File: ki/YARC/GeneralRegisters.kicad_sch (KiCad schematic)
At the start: 12 parts, among them U71 74LS670, U72 74LS670, U73 74LS157, U74 74LS670, U75 74LS670, U76 74LS157, U77 74LS670, U78 74LS670, U79 74LS157, U80 74LS670, U81 74LS670, U82 74LS157

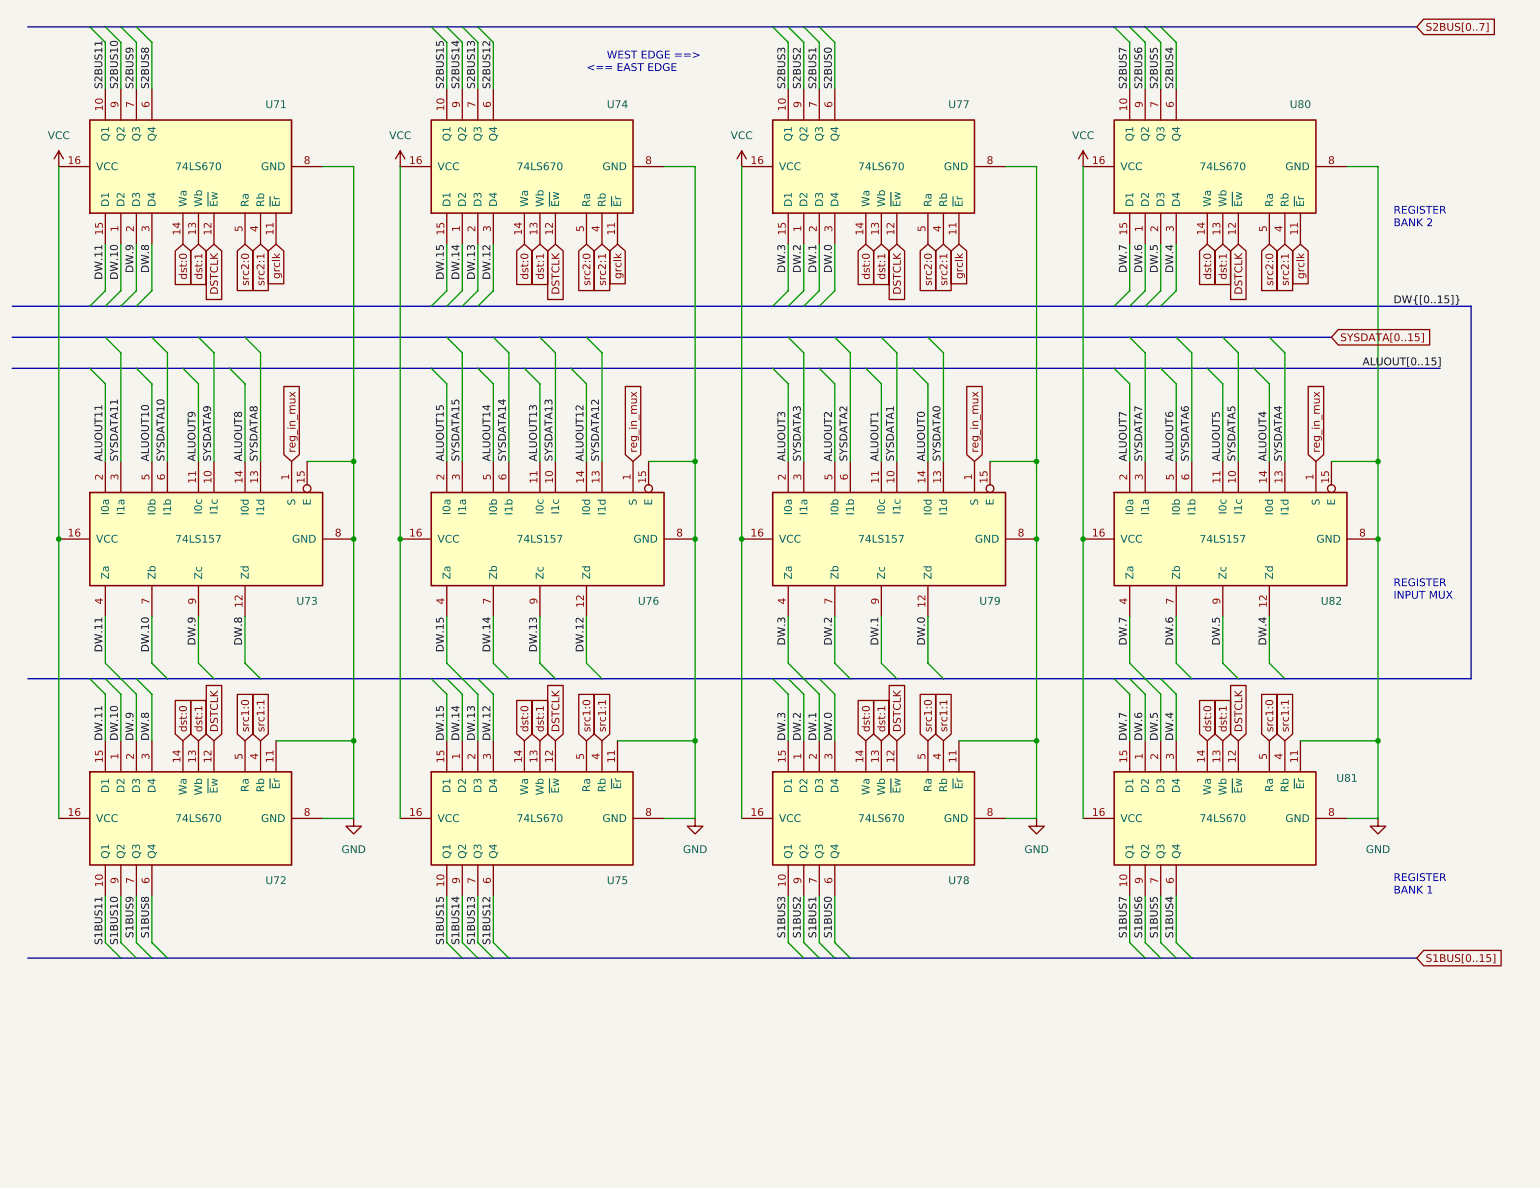
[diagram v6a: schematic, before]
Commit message: Ongoing fixes for ERC errors
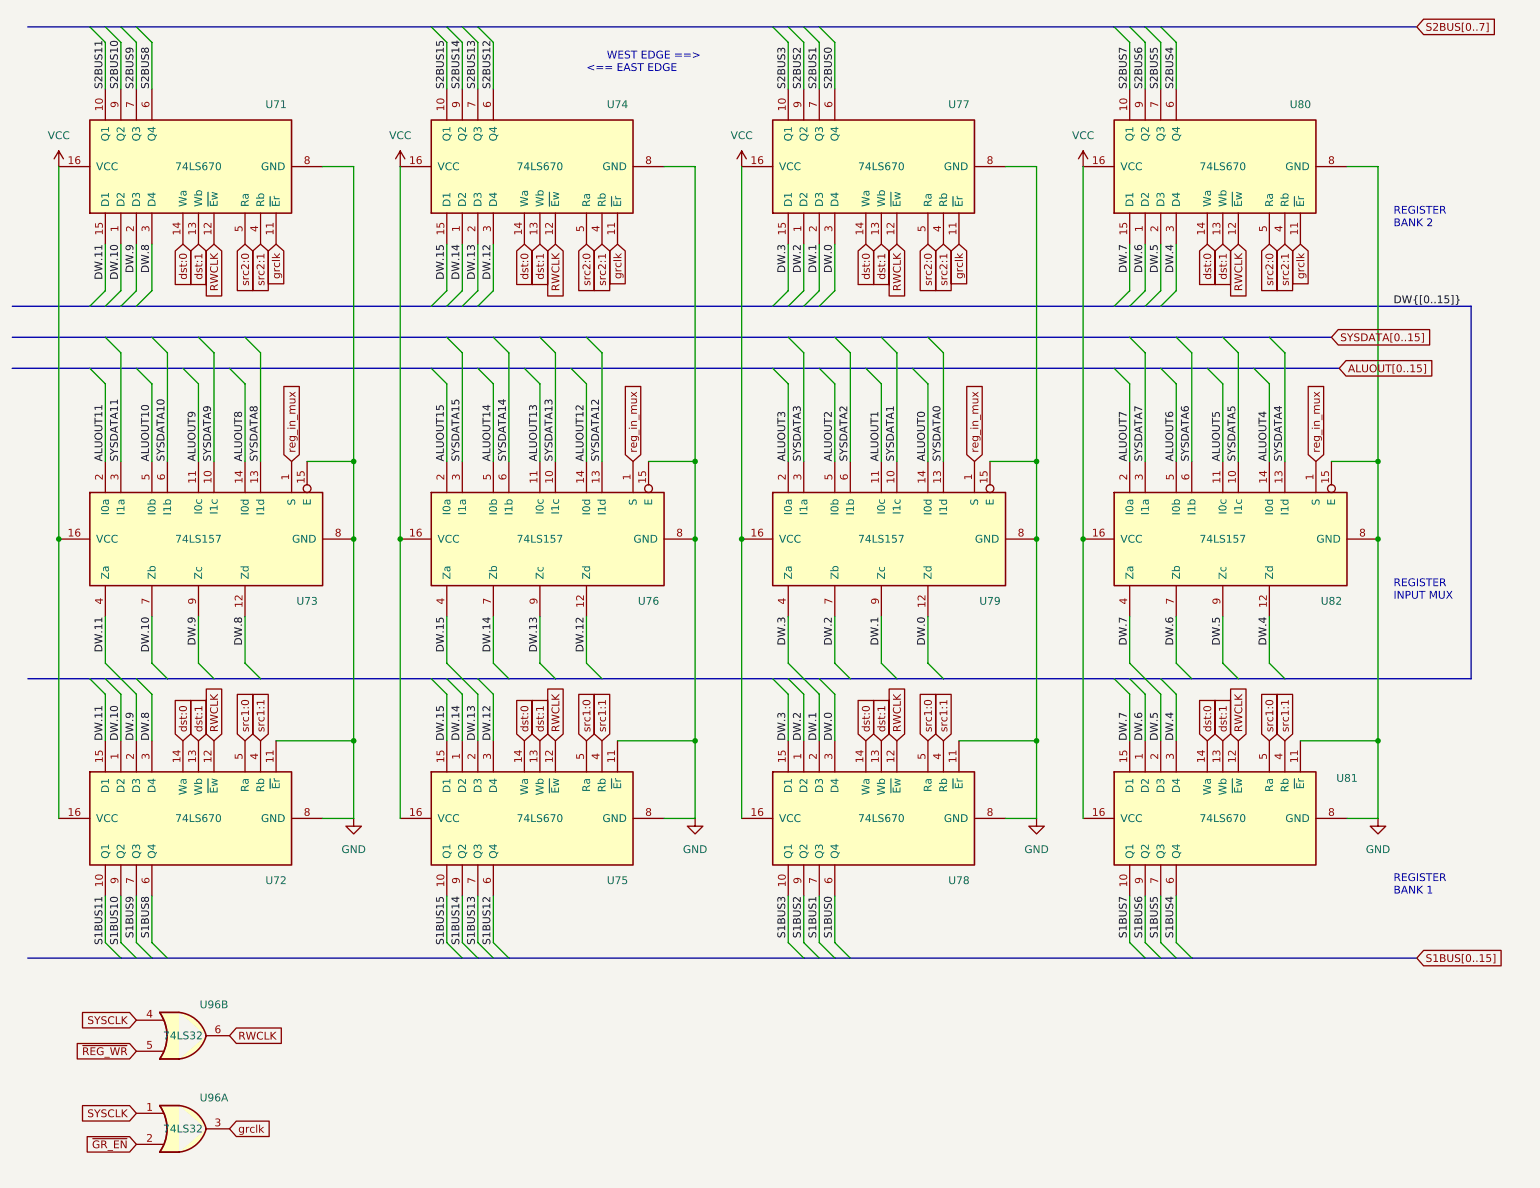
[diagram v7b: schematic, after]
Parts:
- added U96: 74LS32, symbol 74xx:74LS32
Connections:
- net grclk: now also U96.3
- net DSTCLK renamed RWCLK
- net RWCLK: now also U96.6
- new net SYSCLK: U96.1, U96.4
- new net ~{GR_EN}: U96.2
- new net ~{REG_WR}: U96.5
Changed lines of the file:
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@@
     (stroke (width 0) (type default))
   )
-  (bus (pts (xy 218.44 71.12) (xy 248.92 71.12))
+  (bus (pts (xy 218.44 71.12) (xy 232.41 71.12))
     (stroke (width 0) (type default))
   )
@@
     (effects (font (size 1.27 1.27)) (justify right bottom))
   )
-  (label "ALUOUT[0..15]" (at 236.22 71.12 0) (fields_autoplaced)
-    (effects (font (size 1.27 1.27)) (justify left bottom))
-  )
   (label "ALUOUT5" (at 213.36 86.36 90) (fields_autoplaced)
     (effects (font (size 1.27 1.27)) (justify left bottom))
@@
     )
   )
-  (global_label "DSTCLK" (shape input) (at 104.14 132.08 90) (fields_autoplaced)
-    (effects (font (size 1.27 1.27)) (justify left))
-    (property "Intersheetrefs" "${INTERSHEET_REFS}" (at 104.0606 122.6517 90)
+  (global_label "SYSCLK" (shape input) (at 35.56 177.8 180) (fields_autoplaced)
+    (effects (font (size 1.27 1.27)) (justify right))
+    (property "Intersheetrefs" "${INTERSHEET_REFS}" (at 26.0712 177.7206 0)
+      (effects (font (size 1.27 1.27)) (justify right) hide)
+    )
+  )
+  (global_label "RWCLK" (shape input) (at 104.14 132.08 90) (fields_autoplaced)
+    (effects (font (size 1.27 1.27)) (justify left))
+    (property "Intersheetrefs" "${INTERSHEET_REFS}" (at 104.14 122.8053 90)
       (effects (font (size 1.27 1.27)) (justify left) hide)
     )
@@
     )
   )
-  (global_label "DSTCLK" (shape input) (at 160.02 50.8 270) (fields_autoplaced)
-    (effects (font (size 1.27 1.27)) (justify right))
-    (property "Intersheetrefs" "${INTERSHEET_REFS}" (at 159.9406 60.2283 90)
+  (global_label "RWCLK" (shape input) (at 160.02 50.8 270) (fields_autoplaced)
+    (effects (font (size 1.27 1.27)) (justify right))
+    (property "Intersheetrefs" "${INTERSHEET_REFS}" (at 160.02 60.0747 90)
       (effects (font (size 1.27 1.27)) (justify right) hide)
     )
@@
     )
   )
-  (global_label "DSTCLK" (shape input) (at 48.26 132.08 90) (fields_autoplaced)
-    (effects (font (size 1.27 1.27)) (justify left))
-    (property "Intersheetrefs" "${INTERSHEET_REFS}" (at 48.1806 122.6517 90)
-      (effects (font (size 1.27 1.27)) (justify left) hide)
-    )
-  )
-  (global_label "DSTCLK" (shape input) (at 104.14 50.8 270) (fields_autoplaced)
-    (effects (font (size 1.27 1.27)) (justify right))
-    (property "Intersheetrefs" "${INTERSHEET_REFS}" (at 104.0606 60.2283 90)
+  (global_label "RWCLK" (shape input) (at 48.26 132.08 90) (fields_autoplaced)
+    (effects (font (size 1.27 1.27)) (justify left))
+    (property "Intersheetrefs" "${INTERSHEET_REFS}" (at 48.26 122.8053 90)
+      (effects (font (size 1.27 1.27)) (justify left) hide)
+    )
+  )
+  (global_label "RWCLK" (shape input) (at 104.14 50.8 270) (fields_autoplaced)
+    (effects (font (size 1.27 1.27)) (justify right))
+    (property "Intersheetrefs" "${INTERSHEET_REFS}" (at 104.14 60.0747 90)
       (effects (font (size 1.27 1.27)) (justify right) hide)
     )
@@
     )
   )
+  (global_label "RWCLK" (shape input) (at 50.8 180.34 0) (fields_autoplaced)
+    (effects (font (size 1.27 1.27)) (justify left))
+    (property "Intersheetrefs" "${INTERSHEET_REFS}" (at 60.0747 180.34 0)
+      (effects (font (size 1.27 1.27)) (justify left) hide)
+    )
+  )
   (global_label "src2:1" (shape input) (at 55.88 50.8 270) (fields_autoplaced)
     (effects (font (size 1.27 1.27)) (justify right))
@@
     )
   )
+  (global_label "ALUOUT[0..15]" (shape input) (at 232.41 71.12 0) (fields_autoplaced)
+    (effects (font (size 1.27 1.27)) (justify left))
+    (property "Intersheetrefs" "${INTERSHEET_REFS}" (at 249.0025 71.12 0)
+      (effects (font (size 1.27 1.27)) (justify left) hide)
+    )
+  )
   (global_label "src1:0" (shape input) (at 165.1 132.08 90) (fields_autoplaced)
     (effects (font (size 1.27 1.27)) (justify left))
@@
     )
   )
-  (global_label "DSTCLK" (shape input) (at 160.02 132.08 90) (fields_autoplaced)
-    (effects (font (size 1.27 1.27)) (justify left))
-    (property "Intersheetrefs" "${INTERSHEET_REFS}" (at 159.9406 122.6517 90)
+  (global_label "RWCLK" (shape input) (at 160.02 132.08 90) (fields_autoplaced)
+    (effects (font (size 1.27 1.27)) (justify left))
+    (property "Intersheetrefs" "${INTERSHEET_REFS}" (at 160.02 122.8053 90)
       (effects (font (size 1.27 1.27)) (justify left) hide)
     )
@@
     )
   )
-  (global_label "DSTCLK" (shape input) (at 215.9 50.8 270) (fields_autoplaced)
-    (effects (font (size 1.27 1.27)) (justify right))
-    (property "Intersheetrefs" "${INTERSHEET_REFS}" (at 215.8206 60.2283 90)
+  (global_label "RWCLK" (shape input) (at 215.9 50.8 270) (fields_autoplaced)
+    (effects (font (size 1.27 1.27)) (justify right))
+    (property "Intersheetrefs" "${INTERSHEET_REFS}" (at 215.9 60.0747 90)
+      (effects (font (size 1.27 1.27)) (justify right) hide)
+    )
+  )
+  (global_label "SYSCLK" (shape input) (at 35.56 193.04 180) (fields_autoplaced)
+    (effects (font (size 1.27 1.27)) (justify right))
+    (property "Intersheetrefs" "${INTERSHEET_REFS}" (at 26.0712 192.9606 0)
       (effects (font (size 1.27 1.27)) (justify right) hide)
     )
@@
     )
   )
+  (global_label "grclk" (shape input) (at 50.8 195.58 0) (fields_autoplaced)
+    (effects (font (size 1.27 1.27)) (justify left))
+    (property "Intersheetrefs" "${INTERSHEET_REFS}" (at 57.9302 195.5006 0)
+      (effects (font (size 1.27 1.27)) (justify left) hide)
+    )
+  )
   (global_label "dst:1" (shape input) (at 101.6 50.8 270) (fields_autoplaced)
     (effects (font (size 1.27 1.27)) (justify right))
@@
     )
   )
-  (global_label "DSTCLK" (shape input) (at 48.26 50.8 270) (fields_autoplaced)
-    (effects (font (size 1.27 1.27)) (justify right))
-    (property "Intersheetrefs" "${INTERSHEET_REFS}" (at 48.1806 60.2283 90)
+  (global_label "RWCLK" (shape input) (at 48.26 50.8 270) (fields_autoplaced)
+    (effects (font (size 1.27 1.27)) (justify right))
+    (property "Intersheetrefs" "${INTERSHEET_REFS}" (at 48.26 60.0747 90)
+      (effects (font (size 1.27 1.27)) (justify right) hide)
+    )
+  )
+  (global_label "~{REG_WR}" (shape input) (at 35.56 182.88 180) (fields_autoplaced)
+    (effects (font (size 1.27 1.27)) (justify right))
+    (property "Intersheetrefs" "${INTERSHEET_REFS}" (at 25.1968 182.88 0)
       (effects (font (size 1.27 1.27)) (justify right) hide)
     )
@@
     )
   )
-  (global_label "DSTCLK" (shape input) (at 215.9 132.08 90) (fields_autoplaced)
-    (effects (font (size 1.27 1.27)) (justify left))
-    (property "Intersheetrefs" "${INTERSHEET_REFS}" (at 215.8206 122.6517 90)
-      (effects (font (size 1.27 1.27)) (justify left) hide)
+  (global_label "RWCLK" (shape input) (at 215.9 132.08 90) (fields_autoplaced)
+    (effects (font (size 1.27 1.27)) (justify left))
+    (property "Intersheetrefs" "${INTERSHEET_REFS}" (at 215.9 122.8053 90)
+      (effects (font (size 1.27 1.27)) (justify left) hide)
+    )
+  )
+  (global_label "~{GR_EN}" (shape input) (at 35.56 198.12 180) (fields_autoplaced)
+    (effects (font (size 1.27 1.27)) (justify right))
+    (property "Intersheetrefs" "${INTERSHEET_REFS}" (at 27.1598 198.0406 0)
+      (effects (font (size 1.27 1.27)) (justify right) hide)
     )
   )
@@
     )
   )
+  (symbol (lib_id "74xx:74LS32") (at 43.18 180.34 0) (unit 2)
+    (in_bom yes) (on_board yes) (dnp no)
+    (property "Reference" "U96" (at 48.26 175.26 0)
+      (effects (font (size 1.27 1.27)))
+    )
+    (property "Value" "74LS32" (at 43.18 180.34 0)
+      (effects (font (size 1.27 1.27)))
+    )
+    (property "Footprint" "" (at 43.18 180.34 0)
+      (effects (font (size 1.27 1.27)) hide)
+    )
+    (property "Datasheet" "http://www.ti.com/lit/gpn/sn74LS32" (at 43.18 180.34 0)
+      (effects (font (size 1.27 1.27)) hide)
+    )
+    (pin "1")
+    (pin "2")
+    (pin "3")
+    (pin "4")
+    (pin "5")
+    (pin "6")
+    (pin "10")
+    (pin "8")
+    (pin "9")
+    (pin "11")
+    (pin "12")
+    (pin "13")
+    (pin "14")
+    (pin "7")
+    (instances
+      (project "YARC"
+        (path "/22e0f8e1-b0d7-4d47-bb7c-8ef04cd95fca/abd64d43-20ca-4b37-94fd-5fc041c76dd4"
+          (reference "U96") (unit 2)
+        )
+        (path "/22e0f8e1-b0d7-4d47-bb7c-8ef04cd95fca/08911a09-4c52-4bc8-9a9a-ff564ff87689"
+          (reference "U147") (unit 2)
+        )
+      )
+    )
+  )
   (symbol (lib_id "power:VCC") (at 134.62 38.1 0) (unit 1)
     (in_bom yes) (on_board yes) (dnp no) (fields_autoplaced)
@@
         )
       )
+    )
+  )
+  (symbol (lib_id "74xx:74LS32") (at 43.18 195.58 0) (unit 1)
+    (in_bom yes) (on_board yes) (dnp no)
+    (property "Reference" "U96" (at 48.26 190.5 0)
+      (effects (font (size 1.27 1.27)))
+    )
+    (property "Value" "74LS32" (at 43.18 195.58 0)
+      (effects (font (size 1.27 1.27)))
+    )
+    (property "Footprint" "" (at 43.18 195.58 0)
+      (effects (font (size 1.27 1.27)) hide)
+    )
+    (property "Datasheet" "http://www.ti.com/lit/gpn/sn74LS32" (at 43.18 195.58 0)
+      (effects (font (size 1.27 1.27)) hide)
+    )
+    (pin "1")
+    (pin "2")
+    (pin "3")
+    (pin "4")
+    (pin "5")
+    (pin "6")
+    (pin "10")
+    (pin "8")
+    (pin "9")
+    (pin "11")
+    (pin "12")
+    (pin "13")
+    (pin "14")
+    (pin "7")
+    (instances
+      (project "YARC"
+        (path "/22e0f8e1-b0d7-4d47-bb7c-8ef04cd95fca/abd64d43-20ca-4b37-94fd-5fc041c76dd4"
+          (reference "U96") (unit 1)
+        )
+        (path "/22e0f8e1-b0d7-4d47-bb7c-8ef04cd95fca/08911a09-4c52-4bc8-9a9a-ff564ff87689"
+          (reference "U147") (unit 1)
+        )
+      )

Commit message: Continuing cleanup of schematic
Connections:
- net dst:0 renamed DST:0
- net dst:1 renamed DST:1
- net src1:0 renamed SRC1:0
- net src1:1 renamed SRC1:1
- net src2:0 renamed SRC2:0
- net src2:1 renamed SRC2:1
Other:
- note added: "The Register Control Word (RCW) is made up of fields SRC1 (2 bits), SRC2 (3 bits), and DST(3 bits)."
